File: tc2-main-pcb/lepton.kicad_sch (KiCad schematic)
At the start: 34 parts, among them U110 TD6810, U111 TD6810, U112 ME6216A28XG, U113 3N25000G33YC, U114 Flir_LEPTON

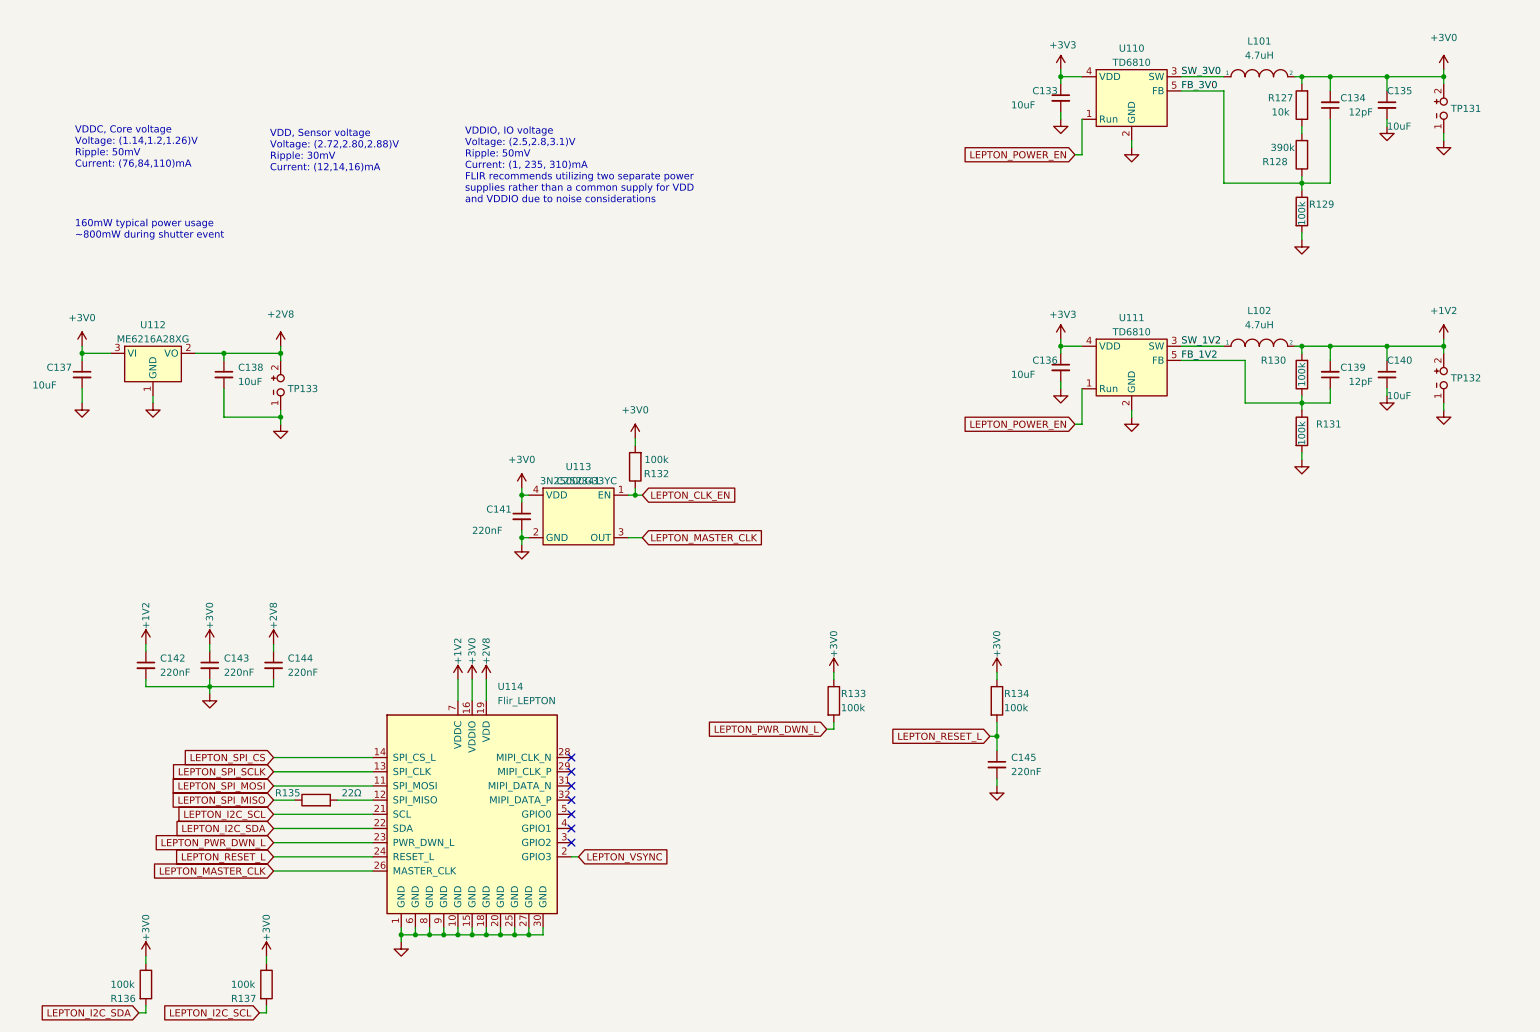
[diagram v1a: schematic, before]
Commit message: Update DC-DC converters
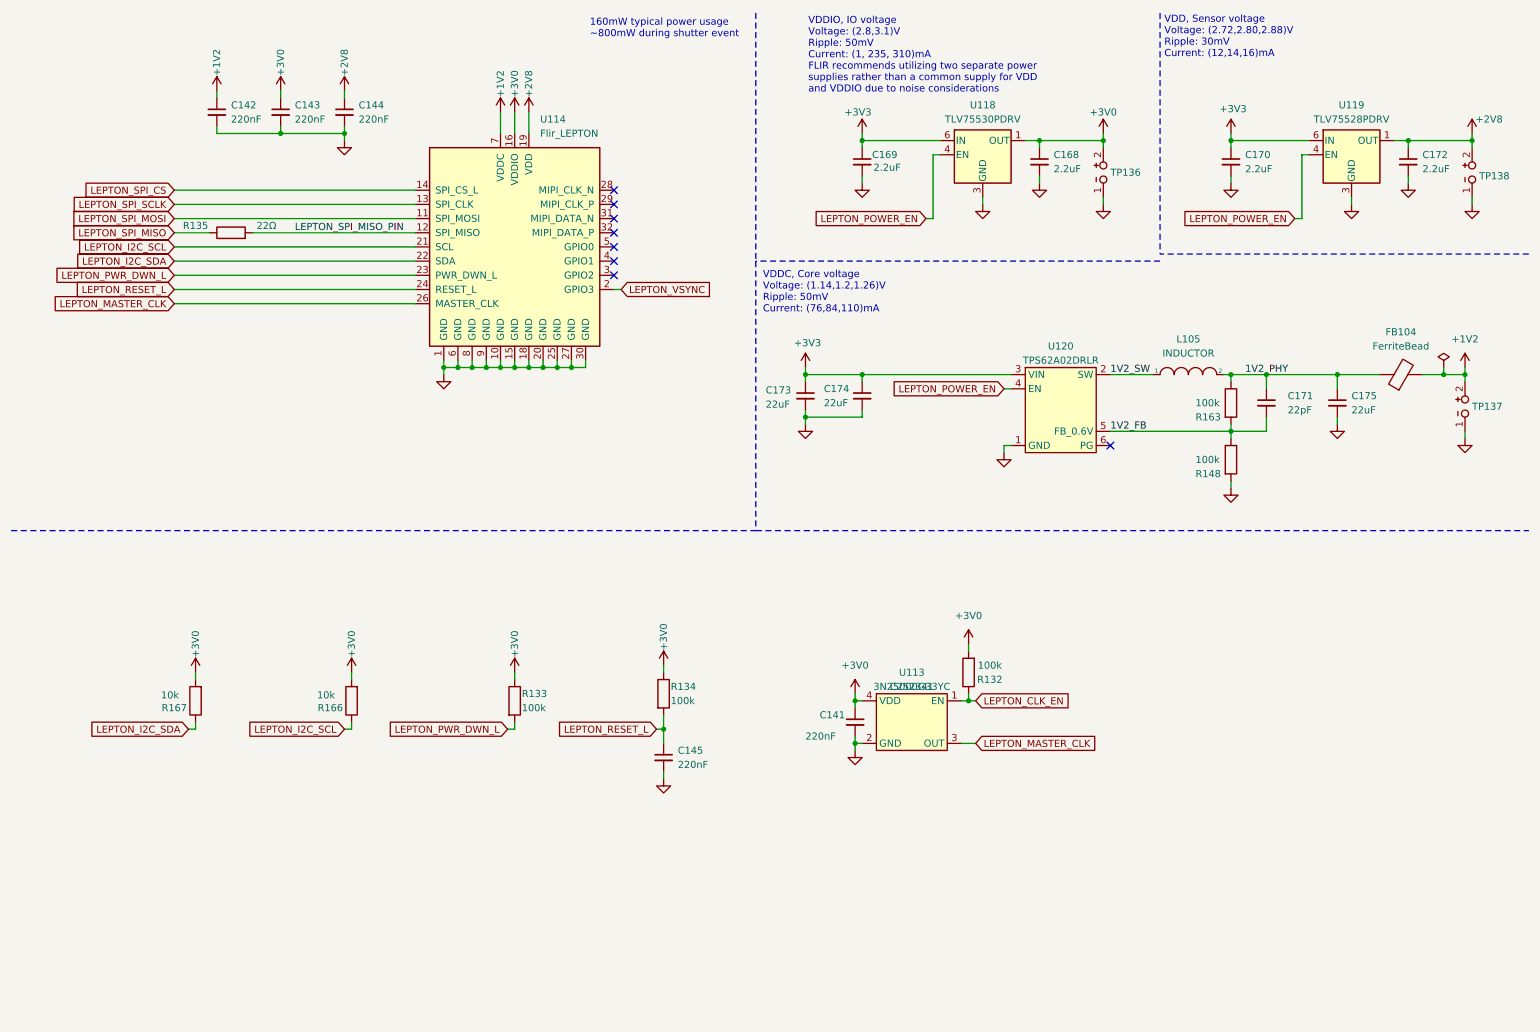
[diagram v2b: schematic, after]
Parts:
- removed C133, C135, C136, C137, C138, C140: 10uF, Capacitor_SMD:C_0603_1608Metric, symbol Device:C_Small
- removed C134, C139: 12pF, Capacitor_SMD:C_0402_1005Metric, symbol Device:C_Small
- removed L101, L102: 4.7uH, cacophony-library:IND-SMD_L4.0-W4.0_SWPA4018S, symbol cacophony-library:Power_Inductor
- removed R127: 10k, Resistor_SMD:R_0402_1005Metric, symbol Device:R
- removed R128: 390k, Resistor_SMD:R_0402_1005Metric, symbol Device:R
- removed R129, R130, R131, R136, R137: 100k, Resistor_SMD:R_0402_1005Metric, symbol Device:R
- removed TP131, TP132, TP133: TP_2P, cacophony-library:test-point-2p, symbol cacophony-library:TestPoint_2Pole
- removed U110, U111: TD6810, cacophony-library:TSOT-23-5, symbol cacophony-library:TD6810
- removed U112: ME6216A28XG, Package_TO_SOT_SMD:TSOT-23, symbol cacophony-library:ME6216A28XG
- added C168, C169, C170, C172: 2.2uF, Capacitor_SMD:C_0402_1005Metric, symbol Device:C_Small
- added C171: 22pF, Capacitor_SMD:C_0402_1005Metric, symbol Device:C_Small
- added C173, C174, C175: 22uF, Capacitor_SMD:C_0603_1608Metric, symbol Device:C_Small
- added FB104: FerriteBead, Inductor_SMD:L_0805_2012Metric, symbol Device:FerriteBead
- added L105: INDUCTOR, Inductor_SMD:L_1008_2520Metric, symbol cacophony-library:Power_Inductor
- added R148, R163: 100k, Resistor_SMD:R_0402_1005Metric, symbol Device:R
- added R166, R167: 10k, Resistor_SMD:R_0402_1005Metric, symbol Device:R
- added TP136, TP137, TP138: TP_2P, cacophony-library:test-point-2p, symbol cacophony-library:TestPoint_2Pole
- added U118: TLV75530PDRV, Package_SON:WSON-6-1EP_2x2mm_P0.65mm_EP1x1.6mm, symbol Regulator_Linear:TLV75530PDRV
- added U119: TLV75528PDRV, Package_SON:WSON-6-1EP_2x2mm_P0.65mm_EP1x1.6mm, symbol Regulator_Linear:TLV75528PDRV
- added U120: TPS62A02DRLR, cacophony-library:SOT-563, symbol cacophony-library:TPS62A02DRLR
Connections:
- net +1V2: now also FB104.2, TP137.2
- net +2V8: now also C172.1, TP138.2, U119.1 (OUT)
- net +3V0: now also C168.1, R166.2, R167.2, TP136.2, U118.1 (OUT)
- net +3V3: now also C169.1, C170.1, C173.1, C174.1, U118.6 (IN), U119.6 (IN), U120.3 (VIN)
- net GND: now also C168.2, C169.2, C170.2, C172.2, C173.2, C174.2, C175.2, R148.2, TP136.1, TP137.1, TP138.1, U118.3 (GND), U118.7 (GND), U119.3 (GND), U119.7 (GND), U120.1 (GND)
- net LEPTON_I2C_SCL: now also R166.1
- net LEPTON_I2C_SDA: now also R167.1
- net LEPTON_POWER_EN: now also U118.4 (EN), U119.4 (EN), U120.4 (EN)
- net LEPTON_SPI_MISO_PIN: now reaches R135.2, U114.12 (SPI_MISO)
- new net 1V2_FB: C171.2, R148.1, R163.2, U120.5 (FB_0.6V)
- new net 1V2_PHY: C171.1, C175.1, FB104.1, L105.2, R163.1
- new net 1V2_SW: L105.1, U120.2 (SW)
- no-connect marks 7 -> 8
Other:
- note added: "VDDIO, IO voltage Voltage: (2.8,3.1)V Ripple: 50mV Current: (1, 235, 310)mA FLIR recommends utilizing two separate power supplies rather than a common supply for VDD and VDDIO due to noise considerations"
- note removed: "VDDIO, IO voltage Voltage: (2.5,2.8,3.1)V Ripple: 50mV Current: (1, 235, 310)mA FLIR recommends utilizing two separate power supplies rather than a common supply for VDD and VDDIO due to noise considerations"
- moved on the sheet: C141, C142, C143, C144, C145, R132, R133, R134, R135, U113, U114

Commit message: Update schematic
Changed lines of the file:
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@@
 	(text "VDDC, Core voltage\nVoltage: (1.14,1.2,1.26)V\nRipple: 50mV\nCurrent: (76,84,110)mA"
 		(exclude_from_sim no)
-		(at 147.32 66.548 0)
+		(at 147.32 65.278 0)
 		(effects
 			(font
@@
 	(polyline
 		(pts
-			(xy 218.44 57.15) (xy 146.05 57.15)
+			(xy 218.44 55.88) (xy 146.05 55.88)
 		)
 		(stroke
@@
 	(polyline
 		(pts
-			(xy 146.05 12.7) (xy 146.05 57.15)
+			(xy 146.05 12.7) (xy 146.05 55.88)
 		)
 		(stroke
@@
 	(polyline
 		(pts
-			(xy 146.05 57.15) (xy 146.05 105.41)
+			(xy 146.05 55.88) (xy 146.05 105.41)
 		)
 		(stroke
@@
 		(property "LCSC Part" "C252341"
 			(at 173.99 133.35 0)
+			(hide yes)
 			(show_name no)
 			(do_not_autoplace no)

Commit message: Update layout
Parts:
- added H1, H2: MountingHole, cacophony-library:MountingHole_1.8mm_M1.6, symbol Mechanical:MountingHole
- added H3, H4: Key Hole, cacophony-library:KeyHole_1.8mm, symbol Mechanical:MountingHole
- added R168: 100k, Resistor_SMD:R_0402_1005Metric, symbol Device:R
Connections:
- net GND: now also R168.2
- net LEPTON_POWER_EN: now also R168.1
